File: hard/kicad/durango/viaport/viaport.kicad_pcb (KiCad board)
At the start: 2 copper layers, 97.8 x 72.4 mm, 18 parts, among them J1 IOx, J2 VIAport, U1 74HC574, U2 74HC574, U3 74HC245, U4 74HC245, U5 74HC174, U6 74HC138, U7 74HC86, U8 74HC245

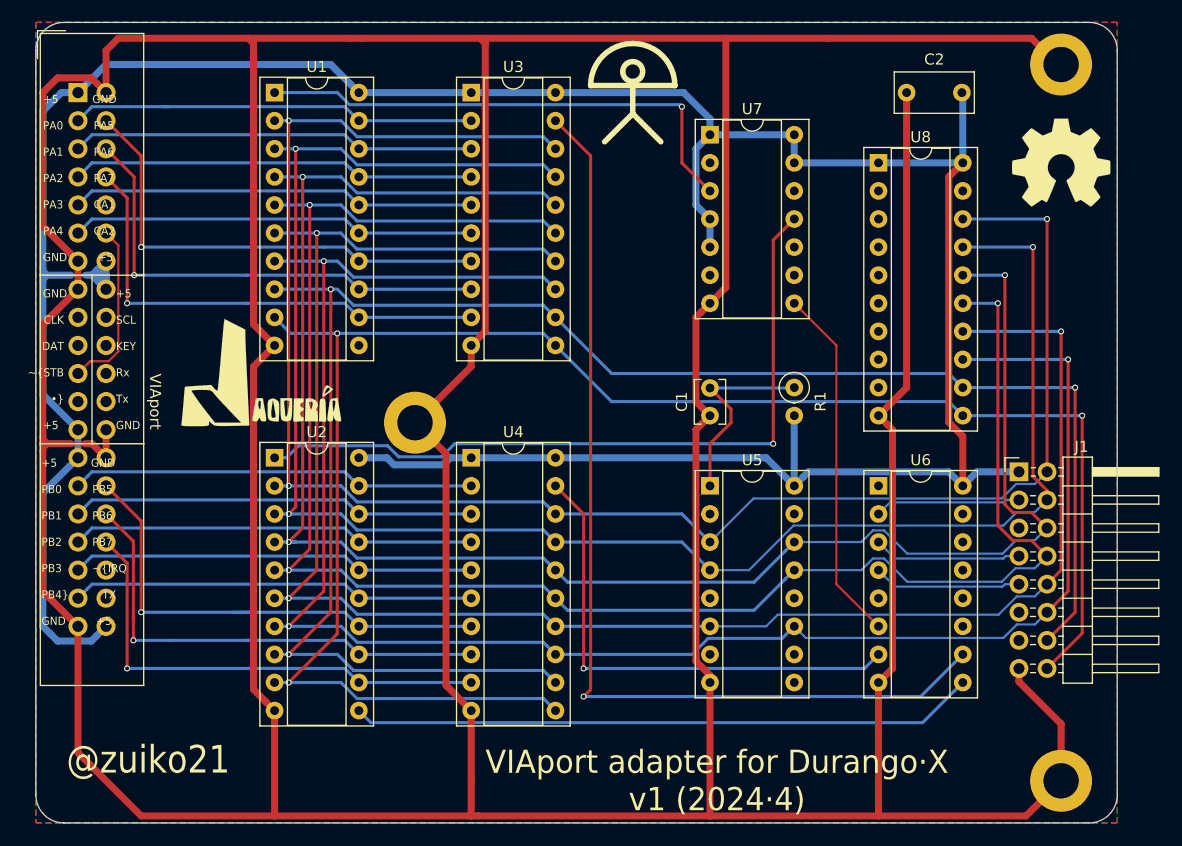
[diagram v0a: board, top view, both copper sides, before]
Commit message: finish VIAport adapter
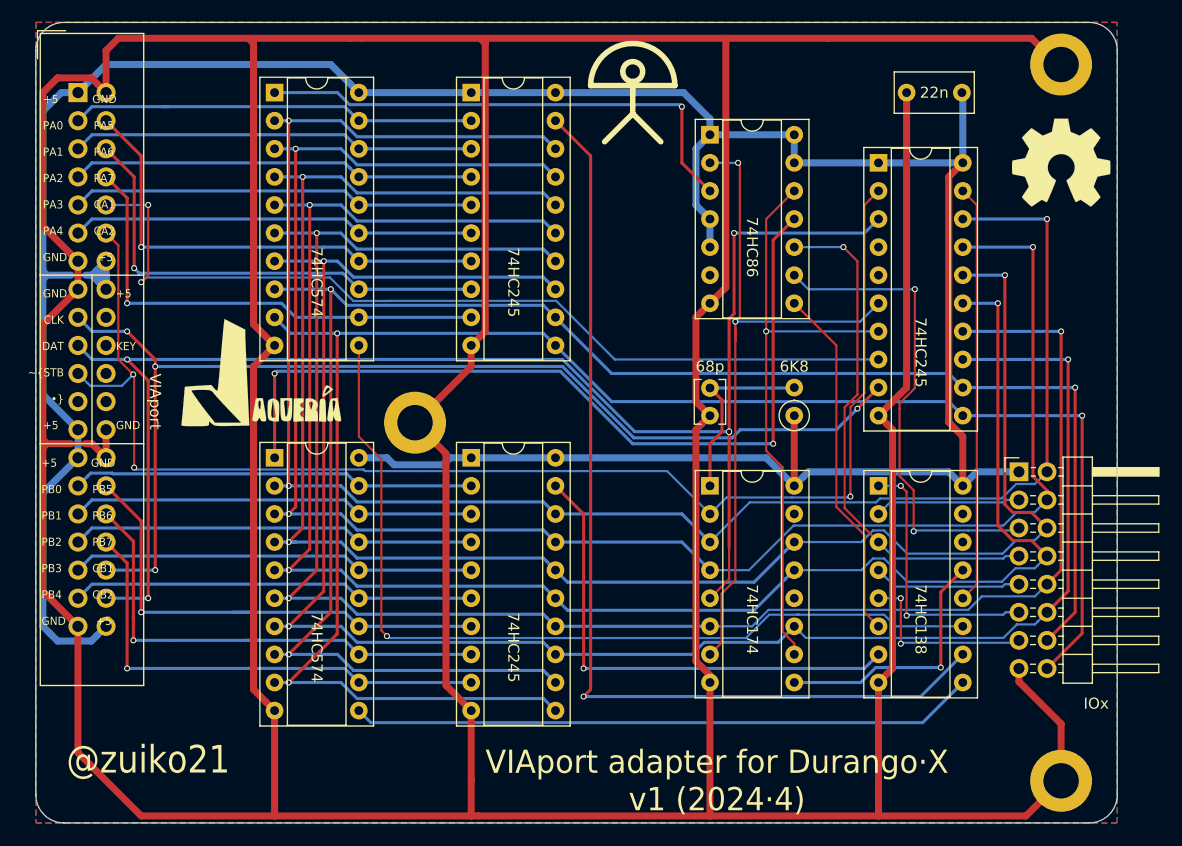
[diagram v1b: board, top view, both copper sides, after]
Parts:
- moved R1 2.54 mm to (87.6, 59.7), turned to 90 degrees
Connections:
- R1 pad 1: /~RST -> +5V
- R1 pad 2: +5V -> /~RST
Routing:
- net /CB2: track 0.80 -> 136.6 mm, vias 0 -> 5
- net /CA2: track 15.6 -> 124.0 mm, vias 0 -> 3
- net /CB1: track 0.00 -> 102.0 mm, vias 0 -> 4
- net /CA1: track 0.00 -> 81.0 mm, vias 0 -> 2
- net /~WRA: track 0.00 -> 81.0 mm, vias 0 -> 1
- net /DDRA: track 0.00 -> 63.1 mm, vias 0 -> 2
- net /DDRB: track 0.00 -> 54.2 mm, vias 0 -> 1
- net /BA1: track 0.00 -> 44.1 mm, vias 0 -> 2
- net /~STAT: track 0.00 -> 37.9 mm
- net /BA2: track 13.4 -> 46.8 mm, vias 0 -> 1
- net /R~W: track 0.00 -> 24.3 mm, vias 0 -> 2
- net /~SET: track 0.00 -> 23.4 mm, vias 0 -> 1
- net /~IOX: track 0.00 -> 16.9 mm, vias 0 -> 2
- net /~DDRB: track 67.6 -> 76.6 mm, vias 1 -> 2
- net /~RST: track 18.1 -> 17.3 mm
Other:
- board text added: "+5 GND PB0 PB5 PB1 PB6 PB2 PB7 PB3 CB1 PB4 CB2 GND +5"
- board text added: "+5 KEY GND"
- board text added: "GND +5 PB5 PB0 PB6 PB1 PB7 PB2 CB1 PB3 CB2 PB4 +5 GND"
- board text removed: "+5 GND PB0 PB5 PB1 PB6 PB2 PB7 PB3 ~IRQ PB4 TX GND +5"
- board text removed: "+5 SCL KEY Rx Tx GND"
- board text removed: "GND +5 PB5 PB0 PB6 PB1 PB7 PB2 IRQ PB3 Tx PB4 +5 GND"

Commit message: add Cx1 pullups to VIAport adapter
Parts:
- added R2: 3K3, Resistor_THT:R_Axial_DIN0207_L6.3mm_D2.5mm_P2.54mm_Vertical, F.Cu at (33.7, 43.2)
- added R3: 3K3, Resistor_THT:R_Axial_DIN0207_L6.3mm_D2.5mm_P2.54mm_Vertical, F.Cu at (33.7, 76.2)
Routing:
- net +5V: track 285.3 -> 303.9 mm
- net /CA1: track 81.0 -> 85.4 mm
- net /CB1: track 102.0 -> 105.8 mm
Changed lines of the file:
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@@
     (thickness 1.6)
     (drawings 32)
-    (tracks 724)
+    (tracks 733)
     (zones 0)
-    (modules 18)
+    (modules 20)
     (nets 49)
   )
@@
   )
   (setup
-    (last_trace_width 0.2)
+    (last_trace_width 0.635)
     (user_trace_width 0.2)
     (user_trace_width 0.28)
@@
     (uvia_dia 0.3)
     (uvia_drill 0.1)
+  )
+  (module Resistor_THT:R_Axial_DIN0207_L6.3mm_D2.5mm_P2.54mm_Vertical (layer F.Cu)
+    (at 33.655 76.2 90)
+    (descr "Resistor, Axial_DIN0207 series, Axial, Vertical, pin pitch=2.54mm, 0.25W = 1/4W, length*diameter=6.3*2.5mm^2, http://cdn-reichelt.de/documents/datenblatt/B400/1_4W%23YAG.pdf")
+    (tags "Resistor Axial_DIN0207 series Axial Vertical pin pitch 2.54mm 0.25W = 1/4W length 6.3mm diameter 2.5mm")
+    (fp_text reference R3 (at 4.445 0 unlocked) (layer B.SilkS)
+      (effects (font (size 1 1) (thickness 0.15)) (justify mirror))
+    )
+    (fp_text value 3K3 (at 4.445 0 unlocked) (layer F.SilkS)
+      (effects (font (size 1 1) (thickness 0.15)))
+    )
+    (fp_line (start 3.59 -1.5) (end -1.5 -1.5) (layer F.CrtYd) (width 0.05))
+    (fp_line (start 3.59 1.5) (end 3.59 -1.5) (layer F.CrtYd) (width 0.05))
+    (fp_line (start -1.5 1.5) (end 3.59 1.5) (layer F.CrtYd) (width 0.05))
+    (fp_line (start -1.5 -1.5) (end -1.5 1.5) (layer F.CrtYd) (width 0.05))
+    (fp_line (start 1.37 0) (end 1.44 0) (layer F.SilkS) (width 0.12))
+    (fp_line (start 0 0) (end 2.54 0) (layer F.Fab) (width 0.1))
+    (fp_circle (center 0 0) (end 1.37 0) (layer F.SilkS) (width 0.12))
+    (fp_circle (center 0 0) (end 1.25 0) (layer F.Fab) (width 0.1))
+    (pad 2 thru_hole oval (at 2.54 0 90) (size 1.6 1.6) (drill 0.8) (layers *.Cu *.Mask)
+      (net 3 /CB1))
+    (pad 1 thru_hole circle (at 0 0 90) (size 1.6 1.6) (drill 0.8) (layers *.Cu *.Mask)
+      (net 2 +5V))
+    (model ${KISYS3DMOD}/Resistor_THT.3dshapes/R_Axial_DIN0207_L6.3mm_D2.5mm_P2.54mm_Vertical.wrl
+      (at (xyz 0 0 0))
+      (scale (xyz 1 1 1))
+      (rotate (xyz 0 0 0))
+    )
+  )
+  (module Resistor_THT:R_Axial_DIN0207_L6.3mm_D2.5mm_P2.54mm_Vertical (layer F.Cu)
+    (at 33.655 43.18 90)
+    (descr "Resistor, Axial_DIN0207 series, Axial, Vertical, pin pitch=2.54mm, 0.25W = 1/4W, length*diameter=6.3*2.5mm^2, http://cdn-reichelt.de/documents/datenblatt/B400/1_4W%23YAG.pdf")
+    (tags "Resistor Axial_DIN0207 series Axial Vertical pin pitch 2.54mm 0.25W = 1/4W length 6.3mm diameter 2.5mm")
+    (fp_text reference R2 (at 4.445 0 unlocked) (layer B.SilkS)
+      (effects (font (size 1 1) (thickness 0.15)) (justify mirror))
+    )
+    (fp_text value 3K3 (at 4.445 0 unlocked) (layer F.SilkS)
+      (effects (font (size 1 1) (thickness 0.15)))
+    )
+    (fp_line (start 3.59 -1.5) (end -1.5 -1.5) (layer F.CrtYd) (width 0.05))
+    (fp_line (start 3.59 1.5) (end 3.59 -1.5) (layer F.CrtYd) (width 0.05))
+    (fp_line (start -1.5 1.5) (end 3.59 1.5) (layer F.CrtYd) (width 0.05))
+    (fp_line (start -1.5 -1.5) (end -1.5 1.5) (layer F.CrtYd) (width 0.05))
+    (fp_line (start 1.37 0) (end 1.44 0) (layer F.SilkS) (width 0.12))
+    (fp_line (start 0 0) (end 2.54 0) (layer F.Fab) (width 0.1))
+    (fp_circle (center 0 0) (end 1.37 0) (layer F.SilkS) (width 0.12))
+    (fp_circle (center 0 0) (end 1.25 0) (layer F.Fab) (width 0.1))
+    (pad 2 thru_hole oval (at 2.54 0 90) (size 1.6 1.6) (drill 0.8) (layers *.Cu *.Mask)
+      (net 37 /CA1))
+    (pad 1 thru_hole circle (at 0 0 90) (size 1.6 1.6) (drill 0.8) (layers *.Cu *.Mask)
+      (net 2 +5V))
+    (model ${KISYS3DMOD}/Resistor_THT.3dshapes/R_Axial_DIN0207_L6.3mm_D2.5mm_P2.54mm_Vertical.wrl
+      (at (xyz 0 0 0))
+      (scale (xyz 1 1 1))
+      (rotate (xyz 0 0 0))
+    )
   )
   (module Package_DIP:DIP-20_W7.62mm_Socket (layer F.Cu)
@@
   (segment (start 78.74 35.56) (end 80.01 34.29) (width 0.635) (layer B.Cu) (net 2))
   (segment (start 78.74 40.64) (end 78.74 35.56) (width 0.635) (layer B.Cu) (net 2))
+  (segment (start 31.996131 76.727499) (end 32.52363 76.2) (width 0.635) (layer B.Cu) (net 2))
+  (segment (start 32.52363 76.2) (end 33.655 76.2) (width 0.635) (layer B.Cu) (net 2))
+  (segment (start 27.412501 76.727499) (end 31.996131 76.727499) (width 0.635) (layer B.Cu) (net 2))
+  (segment (start 25.4 78.74) (end 27.412501 76.727499) (width 0.635) (layer B.Cu) (net 2))
+  (segment (start 27.94 43.18) (end 33.655 43.18) (width 0.635) (layer B.Cu) (net 2))
+  (segment (start 25.4 45.72) (end 27.94 43.18) (width 0.635) (layer B.Cu) (net 2))
   (via (at 29.845 73.66) (size 0.55) (drill 0.35) (layers F.Cu B.Cu) (net 3))
   (segment (start 25.4 73.66) (end 29.845 73.66) (width 0.28) (layer B.Cu) (net 3))
@@
   (segment (start 29.845 55.245) (end 29.845 54.61) (width 0.28) (layer F.Cu) (net 3))
   (segment (start 29.845 73.66) (end 29.845 55.245) (width 0.28) (layer F.Cu) (net 3))
+  (segment (start 29.845 73.66) (end 33.655 73.66) (width 0.28) (layer B.Cu) (net 3))
   (segment (start 25.4 43.18) (end 26.513601 44.293601) (width 0.2) (layer F.Cu) (net 4))
   (segment (start 76.13251 64.70251) (end 56.11507 64.70251) (width 0.2) (layer B.Cu) (net 4))
@@
   (segment (start 48.26 33.02) (end 58.42 33.02) (width 0.28) (layer B.Cu) (net 20))
   (segment (start 25.965 76.765) (end 25.4 76.2) (width 0.2) (layer B.Cu) (net 21))
-  (via (at 29.21 76.2) (size 0.55) (drill 0.35) (layers F.Cu B.Cu) (net 21))
-  (segment (start 25.4 76.2) (end 29.21 76.2) (width 0.28) (layer B.Cu) (net 21))
-  (segment (start 29.21 76.2) (end 29.21 56.515) (width 0.28) (layer F.Cu) (net 21))
   (via (at 27.305 54.61) (size 0.55) (drill 0.35) (layers F.Cu B.Cu) (net 21))
   (segment (start 29.21 56.515) (end 27.305 54.61) (width 0.28) (layer F.Cu) (net 21))
@@
   (segment (start 27.305 54.61) (end 66.675 54.61) (width 0.28) (layer B.Cu) (net 21))
   (via (at 81.740009 61.134991) (size 0.55) (drill 0.35) (layers F.Cu B.Cu) (net 21))
+  (via (at 29.21 75.565) (size 0.55) (drill 0.35) (layers F.Cu B.Cu) (net 21))
+  (segment (start 29.21 75.565) (end 29.21 56.515) (width 0.28) (layer F.Cu) (net 21))
+  (segment (start 26.035 75.565) (end 25.4 76.2) (width 0.28) (layer B.Cu) (net 21))
+  (segment (start 29.21 75.565) (end 26.035 75.565) (width 0.28) (layer B.Cu) (net 21))
   (segment (start 80.01 57.19) (end 87.59 57.19) (width 0.28) (layer B.Cu) (net 22))
   (segment (start 80.01 62.23) (end 80.01 66.04) (width 0.28) (layer F.Cu) (net 22))
@@
   (segment (start 29.21 46.99) (end 29.21 40.64) (width 0.2) (layer F.Cu) (net 37))
   (segment (start 29.21 40.64) (end 25.4 40.64) (width 0.2) (layer B.Cu) (net 37))
+  (segment (start 29.21 40.64) (end 33.655 40.64) (width 0.28) (layer B.Cu) (net 37))
   (segment (start 96.804002 78.74) (end 95.754001 77.689999) (width 0.2) (layer B.Cu) (net 38))
   (segment (start 102.87 78.74) (end 96.804002 78.74) (width 0.2) (layer B.Cu) (net 38))
